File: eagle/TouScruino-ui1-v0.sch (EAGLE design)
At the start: 49 parts, among them J1 AVR_ISP, Q1 8MHz, Q2 MMBT2222, Q3 8MHz, U1 ATMEGA1284P, U3 ARDUINO_SHIELD, U4 MCP73831, U5 MIC5209-3.3YS, X1 USBSMD

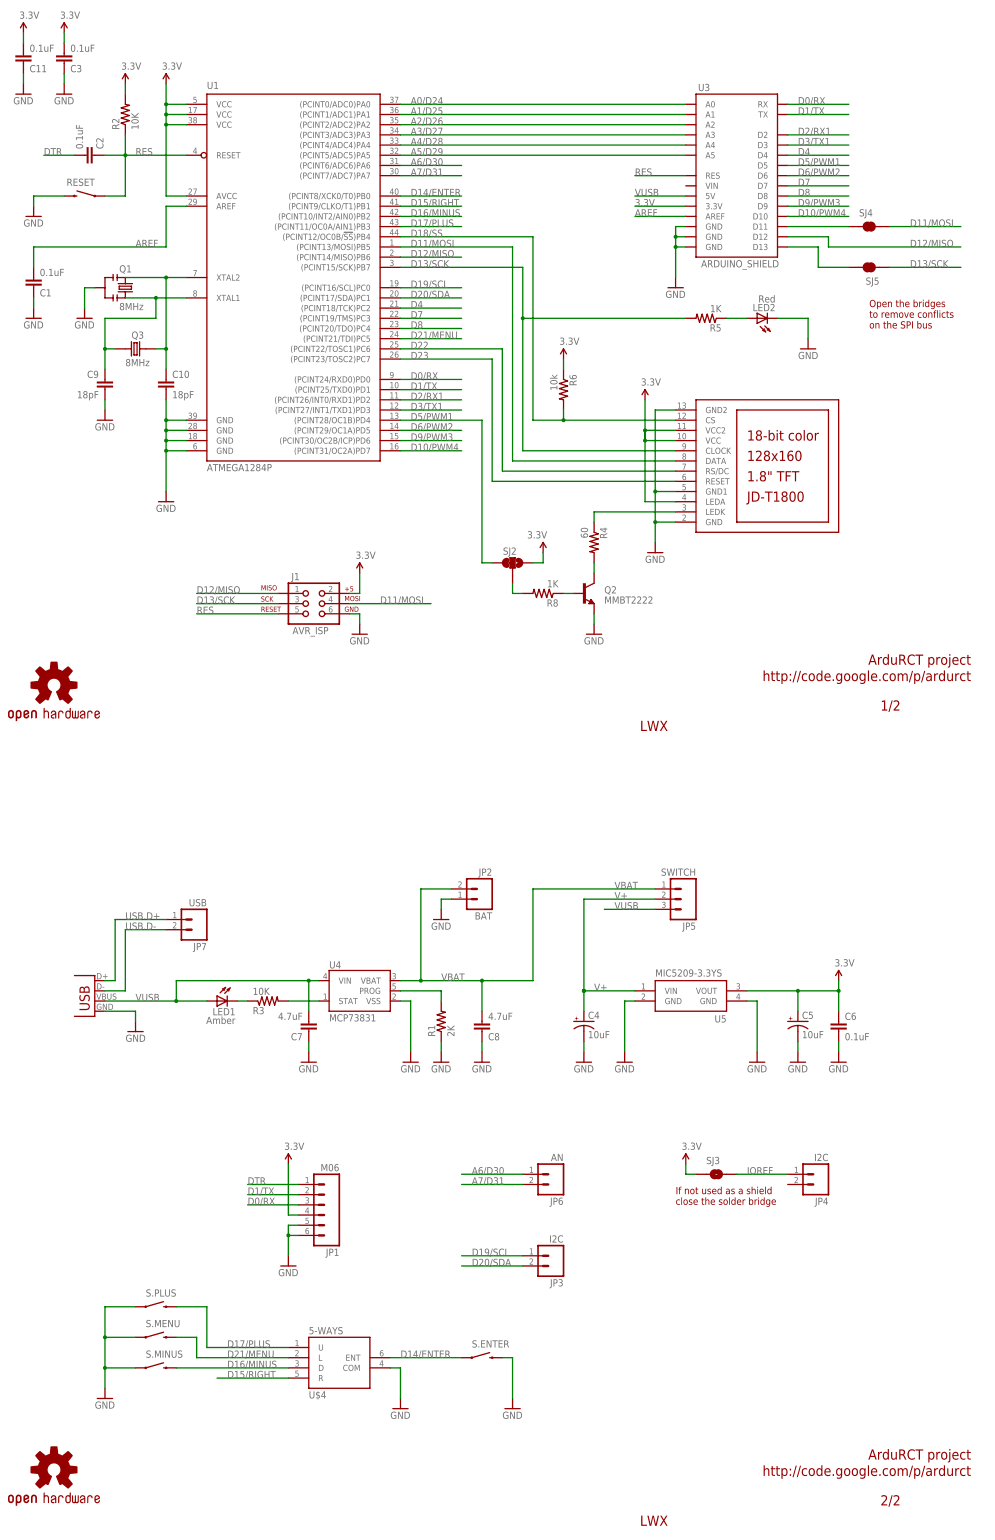
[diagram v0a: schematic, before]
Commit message: 
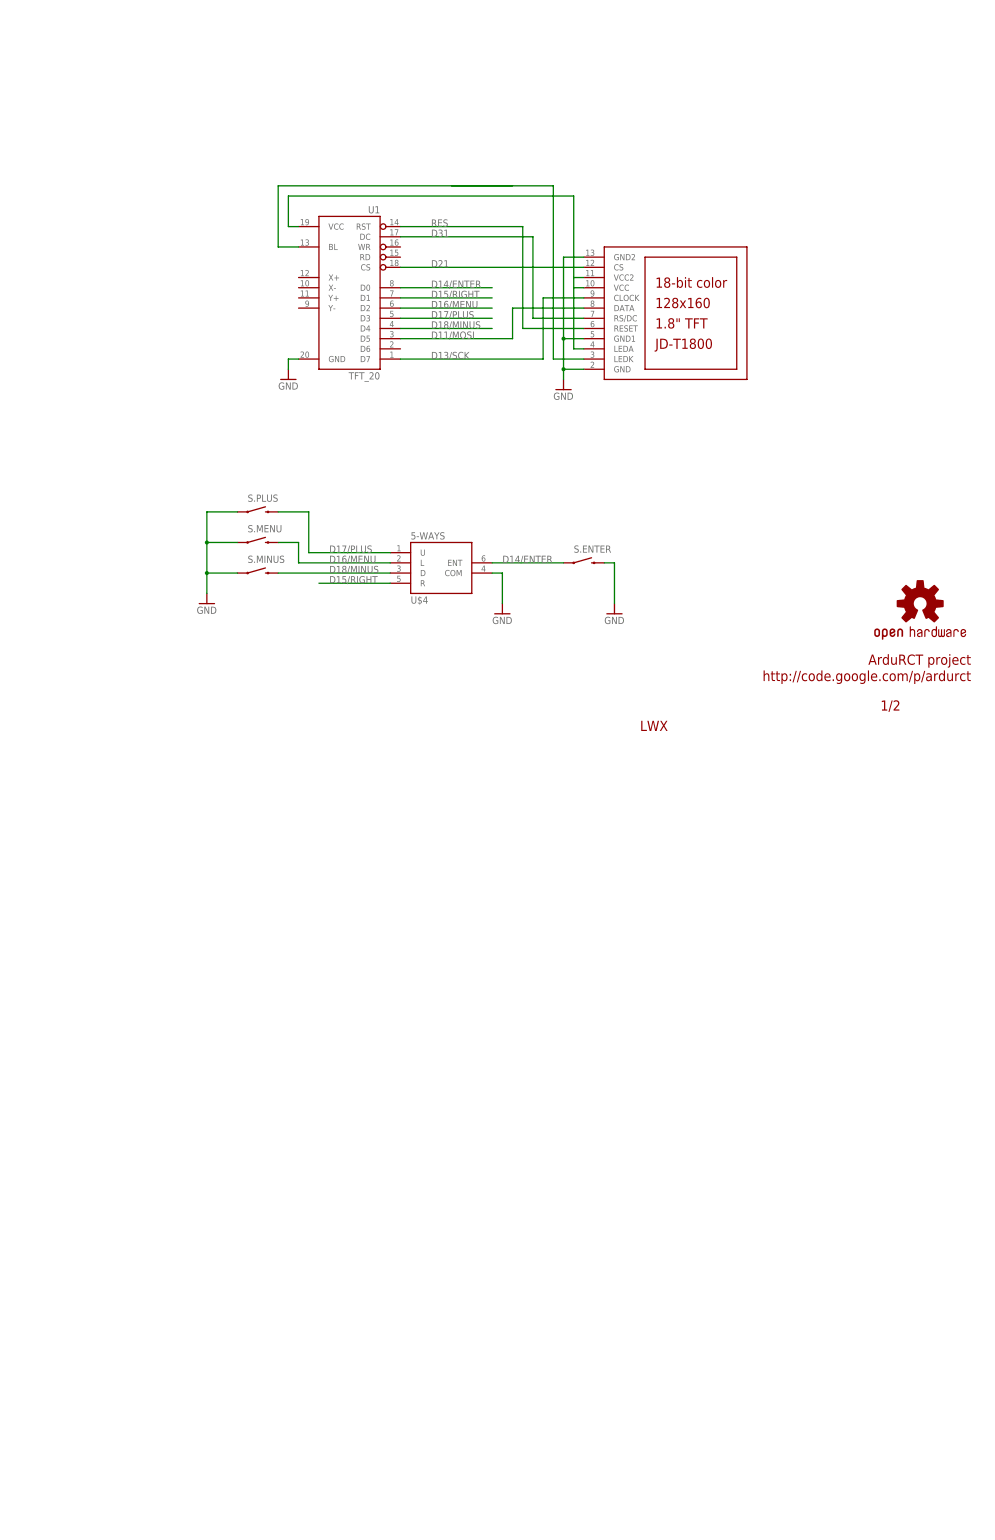
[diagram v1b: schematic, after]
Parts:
- removed C1, C11, C2, C3, C6: 0.1uF, SparkFun:CAP0805
- removed C10, C9: 18pF, SparkFun:CAP0603-CAP
- removed C4, C5: 10uF, SparkFun:CAP_POL1206
- removed C7, C8: 4.7uF, SparkFun:CAP0805
- removed J1: AVR_ISP, SparkFun:AVR_SPI_PRG_6PTH
- removed JP1: M06, wibauxl:M06
- removed JP2: BAT, SparkFun:M02-JST-2MM-SMT
- removed JP3, JP4: I2C, wibauxl:M02
- removed JP5: SWITCH, wibauxl:M03
- removed JP6: AN, wibauxl:M02
- removed JP7: USB, wibauxl:M02
- removed LED1: Amber, wibauxl:LED
- removed LED2: Red, wibauxl:LED805
- removed Q1: 8MHz, SparkFun:RESONATORSMD
- removed Q2: MMBT2222, SparkFun:TRANSISTOR_NPNSOT23-3
- removed Q3: 8MHz, wibauxl:CRYSTAL_5X3.2
- removed R1: 2K, SparkFun:RESISTOR0805-RES
- removed R2, R3: 10K, SparkFun:RESISTOR0805-RES
- removed R4: 60, SparkFun:RESISTOR0805-RES
- removed R5, R8: 1K, SparkFun:RESISTOR0805-RES
- removed R6: 10k, SparkFun:RESISTOR0805-RES
- removed RESET: SWITCH-MOMENTARY-2SMD, SparkFun:SWITCH-MOMENTARY-2SMD
- removed SJ2: SJ_2WAYS_1-2, wibauxl:SJ_2WAYS_1-2
- removed SJ3: SOLDERJUMPERNO, SparkFun:SOLDERJUMPERNO
- removed SJ4, SJ5: SOLDERJUMPERTRACE, SparkFun:SOLDERJUMPERTRACE
- removed U$5: OSHW-LOGOM, SparkFun:OSHW-LOGOM
- removed U3: ARDUINO_SHIELD, wibauxl:ARDUINO_SHIELD
- removed U4: MCP73831, SparkFun:MCP73831
- removed U5: MIC5209-3.3YS, wibauxl:MIC5209
- removed X1: USBSMD, SparkFun:USBSMD
- U1: value ATMEGA1284P -> TFT_20; device wibauxl:ATMEGA324A -> wibauxl:TFT_20
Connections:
- removed net 3.3V: C11.2, C3.2, C5.+, C6.1, J1.2, JP1.4, LCD1.LEDA, LCD1.VCC, LCD1.VCC2, R2.2, R6.1, SJ2.3, SJ3.1, U1.AVCC, U1.VCC, U1.VCC@1, U1.VCC@2, U3.3.3V, U5.VOUT
- removed net A0/D24: U1.(PCINT0/ADC0)PA0, U3.A0
- removed net A1/D25: U1.(PCINT1/ADC1)PA1, U3.A1
- removed net A2/D26: U1.(PCINT2/ADC2)PA2, U3.A2
- removed net A3/D27: U1.(PCINT3/ADC3)PA3, U3.A3
- removed net A4/D28: U1.(PCINT4/ADC4)PA4, U3.A4
- removed net A5/D29: U1.(PCINT5/ADC5)PA5, U3.A5
- removed net A6/D30: JP6.1, U1.(PCINT6/ADC6)PA6
- removed net A7/D31: JP6.2, U1.(PCINT7/ADC7)PA7
- removed net AREF: C1.2, U1.AREF, U3.AREF
- removed net BL_CMD: R8.2, SJ2.2
- removed net D0/RX: JP1.3, U1.(PCINT24/RXD0)PD0, U3.RX
- removed net D1/TX: JP1.2, U1.(PCINT25/TXD0)PD1, U3.TX
- removed net D10/PWM4: U1.(PCINT31/OC2A)PD7, U3.D10
- removed net D12/MISO: J1.1, U1.(PCINT14/MISO)PB6, U3.D12
- removed net D16/MINUS: S.MINUS.2, U$4.D, U1.(PCINT10/INT2/AIN0)PB2
- removed net D18/SS: LCD1.CS, R6.2, U1.(PCINT12/OC0B/!SS!)PB4
- removed net D19/SCL: JP3.1, U1.(PCINT16/SCL)PC0
- removed net D2/RX1: U1.(PCINT26/INT0/RXD1)PD2, U3.D2
- removed net D20/SDA: JP3.2, U1.(PCINT17/SDA)PC1
- removed net D21/MENU: S.MENU.2, U$4.L, U1.(PCINT21/TDI)PC5
- removed net D22: LCD1.RS/DC, U1.(PCINT22/TOSC1)PC6
- removed net D23: LCD1.RESET, U1.(PCINT23/TOSC2)PC7
- removed net D3/TX1: U1.(PCINT27/INT1/TXD1)PD3, U3.D3
- removed net D4: U1.(PCINT18/TCK)PC2, U3.D4
- removed net D5/PWM1: SJ2.1, U1.(PCINT28/OC1B)PD4, U3.D5
- removed net D6/PWM2: U1.(PCINT29/OC1A)PD5, U3.D6
- removed net D7: U1.(PCINT19/TMS)PC3, U3.D7
- removed net D8: U1.(PCINT20/TDO)PC4, U3.D8
- removed net D9/PWM3: U1.(PCINT30/OC2B/ICP)PD6, U3.D9
- removed net DTR: C2.2, JP1.1
- removed net IOREF: JP4.1, SJ3.2
- removed net N$1: C9.1, Q1.1, Q3.2, U1.XTAL1
- removed net N$12: R3.2, U4.STAT
- removed net N$13: R1.2, U4.PROG
- removed net N$17: Q2.C, R4.2
- removed net N$2: C10.1, Q1.3, Q3.1, U1.XTAL2
- removed net N$3: LCD1.LEDK, R4.1
- removed net N$4: Q2.B, R8.1
- removed net N$5: LED2.A, R5.1
- removed net N$6: SJ4.1, U3.D11
- removed net N$8: LED1.C, R3.1
- removed net N$9: SJ5.2, U3.D13
- removed net USB.D+: JP7.1, X1.D+
- removed net USB.D-: JP7.2, X1.D-
- removed net V+: C4.+, JP5.2, U5.VIN
- removed net VBAT: C8.2, JP2.2, JP5.1, U4.VBAT
- removed net VUSB: C7.2, JP5.3, LED1.A, U3.5V, U4.VIN, X1.VBUS
- new net BL: LCD1.LEDK, U1.BL
- new net D16/MENU: S.MENU.2, U$4.L, U1.D2
- new net D18/MINUS: S.MINUS.2, U$4.D, U1.D4
- new net D21: LCD1.CS, U1.CS
- new net D31: LCD1.RS/DC, U1.DC
- new net VCC: LCD1.LEDA, LCD1.VCC, LCD1.VCC2, U1.VCC
- net D11/MOSI: now also U1.D5; no longer J1.4, SJ4.2, U1.(PCINT13/MOSI)PB5
- net D13/SCK: now also U1.D7; no longer J1.3, R5.2, SJ5.1, U1.(PCINT15/SCK)PB7
- net D14/ENTER: now also U1.D0; no longer U1.(PCINT8/XCK0/T0)PB0
- net D15/RIGHT: now also U1.D1; no longer U1.(PCINT9/CLKO/T1)PB1
- net D17/PLUS: now also U1.D3; no longer U1.(PCINT11/OC0A/AIN1)PB3
- net GND: no longer C1.1, C10.2, C11.1, C3.1, C4.-, C5.-, C6.2, C7.1, C8.1, C9.2, J1.6, JP1.5, JP1.6, JP2.1, LED2.C, Q1.2, Q2.E, R1.1, RESET.2, U1.GND@1, U1.GND@2, U1.GND@3, U3.GND@0, U3.GND@1, U3.GND@2, U4.VSS, U5.GND@1, U5.GND@2, X1.GND
- net RES: now also LCD1.RESET, U1.RST; no longer C2.1, J1.5, R2.1, RESET.1, U1.RESET, U3.RES
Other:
- note removed: "2/2"
- note removed: "If not used as a shield close the solder bridge"
- note removed: "Open the bridges to remove conflicts on the SPI bus"
- moved on the sheet: S.ENTER, S.MENU, S.MINUS, S.PLUS, U$4
